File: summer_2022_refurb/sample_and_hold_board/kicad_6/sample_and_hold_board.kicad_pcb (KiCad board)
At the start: 2 copper layers, 40.6 x 203.2 mm, 107 parts, among them J1 VCO_port, J2 VCF_port, J3 ribbon_port, J4 power_entry, Q1 MMBT3904, Q2 2N3904, Q3 MMBT3904, SW1 SW_SPDT, U1 TL072, U2 TL072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

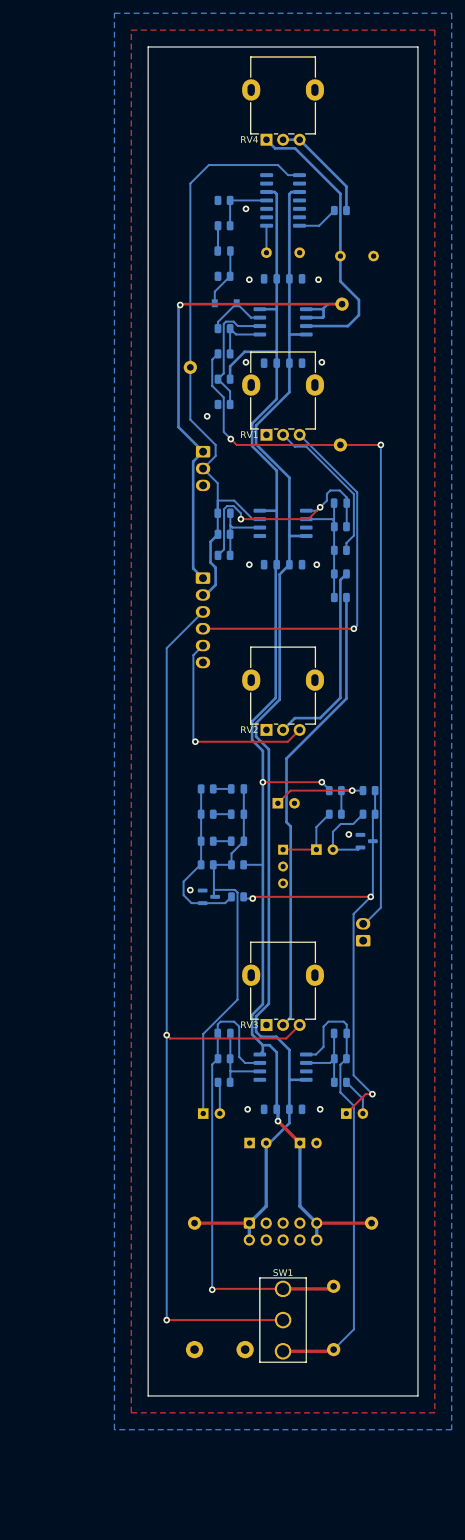
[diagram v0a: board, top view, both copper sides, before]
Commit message: Update sample and hold board
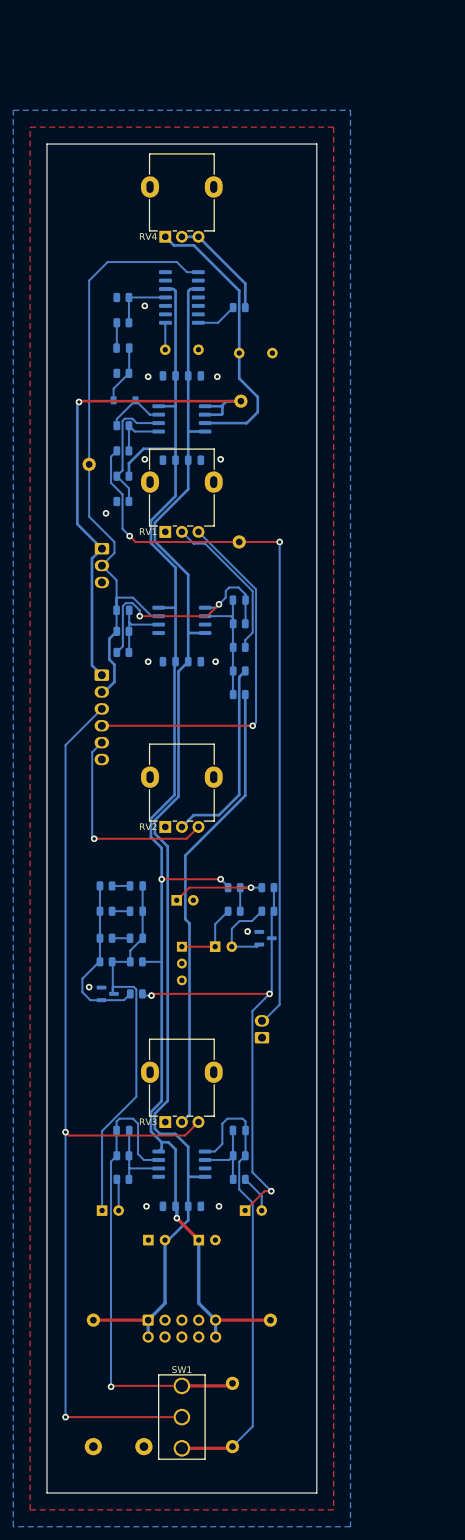
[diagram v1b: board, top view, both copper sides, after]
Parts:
- R7: value 22 -> 47
- moved C10 21.1 mm to (97.3, 152.0)
- moved C11 21.1 mm to (92.1, 193.1)
- moved C20 21.1 mm to (99.1, 197.5)
- moved C6 21.1 mm to (109.2, 153.3)
- moved C7 21.1 mm to (97.3, 144.2)
- moved C9 21.1 mm to (97.3, 148.0)
- moved R11 21.1 mm to (112.0, 148.0)
- moved R12 21.1 mm to (117.1, 148.0)
- moved R13 21.1 mm to (97.3, 155.6)
- moved R14 21.1 mm to (97.3, 160.4)
- moved R15 21.1 mm to (92.7, 144.2)
- moved R16 21.1 mm to (92.7, 148.0)
- moved R18 21.1 mm to (92.7, 152.0)
- moved R20 21.1 mm to (92.7, 155.6)
- moved TP6 21.1 mm to (117.5, 209.6)
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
